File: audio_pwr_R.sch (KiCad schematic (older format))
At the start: 43 parts, among them Q201 BC546, Q202 BC546, Q203 BC546, Q204 BD140, Q205 BC546, Q206 BD139, Q207 BD140, Q208 MJL21193, Q209 MJL21194

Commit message: Lots of part changes to SMD devices. Adding MPN, MFG to all parts for BOM export.
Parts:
- removed F201, F202: 3A, Fuseholders:Fuseholder5x20_horiz_open_inline_Type-I, symbol Device:Fuse
- removed Q201, Q203: BC546, Package_TO_SOT_THT:TO-92_Inline, symbol AAMB-rescue:BC546-transistors
- added F301, F302: 0154003.DR, Fuse:0154003.DR, symbol Fuse:0154003.DR
- added U301: BC846BDW1T1G, Package_TO_SOT_SMD:SOT-363_SC-70-6, symbol OnSemi_BC846:BC846BDW1T1G
- C201: footprint Capacitor_THT:CP_Radial_D5.0mm_P2.00mm -> Capacitor_SMD:CP_Elec_4x5.4; DigiKey (none) -> https://www.we-online.de/katalog/datasheet/865080640004.pdf; MFG (none) -> Würth Elektronik; MPN (none) -> 865080640004
- C202, C204, C206: footprint Capacitor_THT:C_Disc_D5.1mm_W3.2mm_P5.00mm -> Capacitor_SMD:C_0603_1608Metric_Pad1.05x0.95mm_HandSolder; DigiKey (none) -> https://www.digikey.com/product-detail/en/w%C3%BCrth-elektr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; MFG (none) -> Würth Elektronik; MPN (none) -> 885012006057
- C203: footprint Capacitor_THT:CP_Radial_D10.0mm_P5.00mm -> Capacitor_SMD:C_Elec_5x5.4; DigiKey (none) -> https://www.digikey.com/product-detail/en/w%C3%BCrth-elektr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; MFG (none) -> Würth Elektronik; MPN (none) -> 865080142007
- C205: footprint Capacitor_THT:CP_Radial_D10.0mm_P5.00mm -> Capacitor_SMD:C_Elec_6.3x7.7; DigiKey (none) -> https://www.digikey.com/product-detail/en/w%C3%BCrth-elektr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; MFG (none) -> Würth Elektronik; MPN (none) -> 865080545012
- C207, C208, C209: DigiKey (none) -> https://www.digikey.com/product-detail/en/kemet/R82EC3100AA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; MFG (none) -> KEMET; MPN (none) -> R82EC3100AA70K
- C210, C211: footprint Capacitor_THT:CP_Radial_D10.0mm_P5.00mm -> Capacitor_SMD:CP_Elec_10x10.5; DigiKey (none) -> https://www.digikey.com/product-detail/en/nichicon/UUX1J101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; MFG (none) -> Nichicon; MPN (none) -> UUX1J101MNL1GS
- D201: footprint LED_THT:LED_D3.0mm -> LED_SMD:LED_0603_1608Metric_Pad1.05x0.95mm_HandSolder; DigiKey (none) -> https://www.digikey.com/product-detail/en/rohm-semiconducto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; MFG (none) -> Rohm Semiconductor; MPN (none) -> SML-D12U1WT86
- Q202, Q205: value BC546 -> BC846; footprint Package_TO_SOT_THT:TO-92_Inline -> Package_TO_SOT_SMD:SOT-23; DigiKey (none) -> https://www.digikey.com/product-detail/en/on-semiconductor/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; MFG (none) -> ON Semiconductor; MPN (none) -> BC846BLT1G
- Q204, Q207: value BD140 -> BCP53; footprint Package_TO_SOT_THT:TO-126-3_Vertical -> Package_TO_SOT_SMD:SOT-223; DigiKey (none) -> https://www.digikey.com/product-detail/en/on-semiconductor/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; MFG (none) -> ON Semiconductor; MPN (none) -> SBCP53-10T1G
- Q206: value BD139 -> BCP56; footprint Package_TO_SOT_THT:TO-126-3_Vertical -> Package_TO_SOT_SMD:SOT-223; DigiKey (none) -> https://www.digikey.com/product-detail/en/on-semiconductor/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; MFG (none) -> ON Semiconductor; MPN (none) -> SBCP56-16T3G
- R214, R215: value 15m -> 330m; footprint Resistor_THT:R_Axial_Power_L25.0mm_W9.0mm_P10.16mm_Vertical -> Resistor_THT:R_Radial_Power_L13.0mm_W9.0mm_P5.00mm; DigiKey (none) -> https://www.digikey.com/product-detail/en/te-connectivity-p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; MFG (none) -> TE Connectivity Passive Product; MPN (none) -> SQMW5R33J

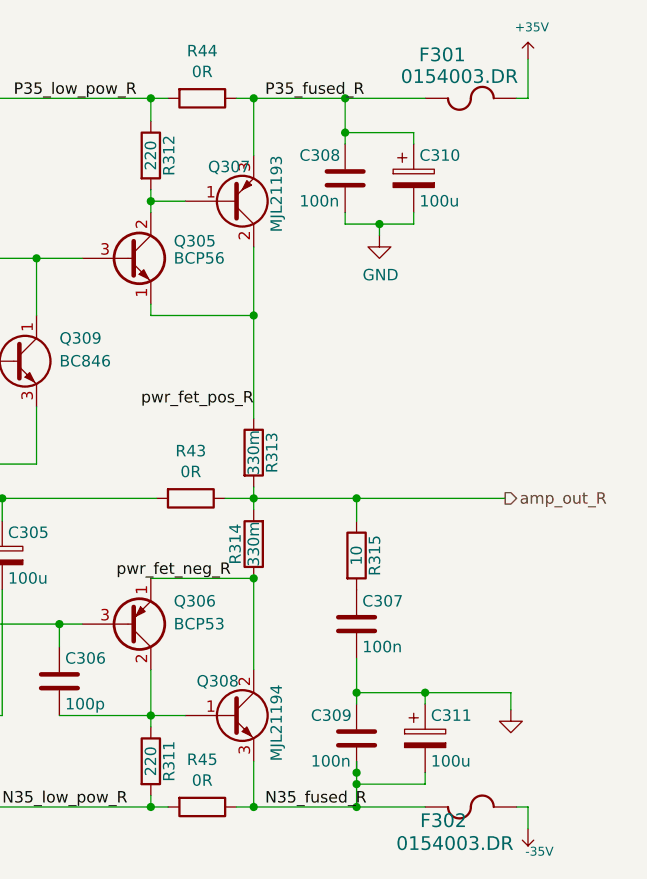
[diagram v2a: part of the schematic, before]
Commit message: Layout startover, sorting, some routing. Removed redundant fuses. BOM export.
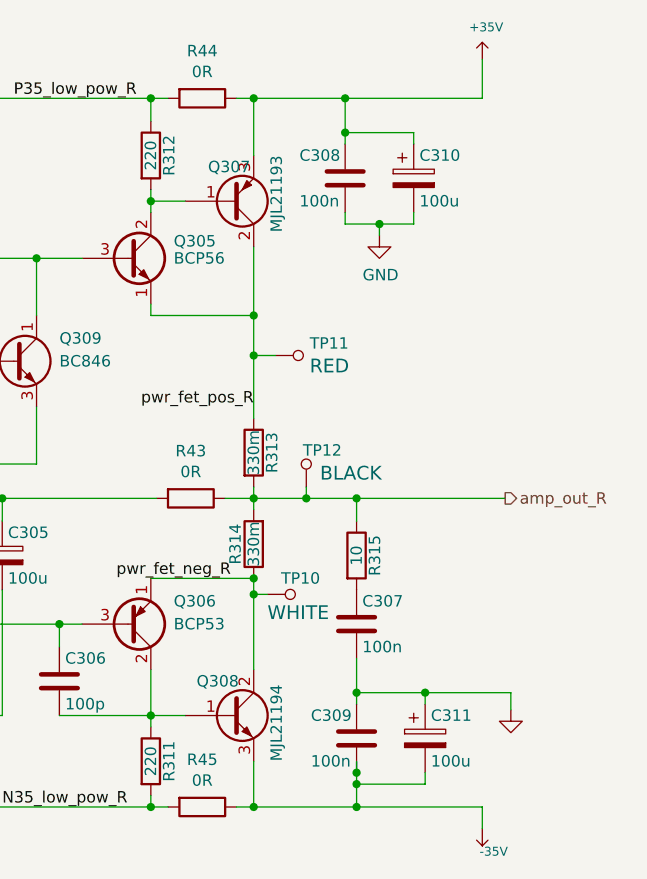
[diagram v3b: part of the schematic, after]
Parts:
- removed F301, F302: 0154003.DR, Fuse:0154003.DR, symbol Fuse:0154003.DR
- added TP10: 5002, digikey-footprints:Test_Point_D1.02mm, symbol dk_Test-Points:5002
- added TP11: 5000, digikey-footprints:Test_Point_D1.02mm, symbol dk_Test-Points:5000
- added TP12: 5001, digikey-footprints:Test_Point_D1.02mm, symbol dk_Test-Points:5001
- C201, C202, C203, C204, C205, C206: MFG Würth Elektronik -> Wurth Elektronik
- Q208: DigiKey (none) -> https://www.digikey.com/products/en/discrete-semiconductor-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; MFG (none) -> ON Semiconductor; MPN (none) -> MJL21193G
- Q209: DigiKey (none) -> https://www.digikey.com/products/en/discrete-semiconductor-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; MFG (none) -> ON Semiconductor; MPN (none) -> MJL21194G
- R201, R203, R207, R209: DigiKey (none) -> https://www.digikey.com/product-detail/en/vishay-dale/RCS06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; MFG (none) -> Vishay Dale; MPN (none) -> RCS06031K00FKEA
- R202, R204, R208: DigiKey (none) -> https://www.digikey.com/product-detail/en/te-connectivity-p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; MFG (none) -> TE Connectivity Passive Product; MPN (none) -> CRGCQ0603F22K
- R205, R206: DigiKey (none) -> https://www.digikey.com/product-detail/en/te-connectivity-p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; MFG (none) -> TE Connectivity Passive Product; MPN (none) -> CRGCQ0603F560R
- R210, R211: DigiKey (none) -> https://www.digikey.com/product-detail/en/vishay-dale/CRCW0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; MFG (none) -> Vishay Dale; MPN (none) -> CRCW06033K30FKEA
- R212, R213: DigiKey (none) -> https://www.digikey.com/product-detail/en/panasonic-electro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; MFG (none) -> Panasonic Electronic Components; MPN (none) -> ERJ-PA3F2200V
- R216: DigiKey (none) -> https://www.digikey.com/product-detail/en/panasonic-electro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; MFG (none) -> Panasonic Electronic Components; MPN (none) -> ERJ-PA3F10R0V
- R43, R44, R45: MFG (none) -> Stackpole Electronics Inc; MPN (none) -> RMCF1210ZT0R00
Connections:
- net N35_fused_R is gone; now on net -35V: C209.2, C211.2, Q209.3 (E), R45.1
- net P35_fused_R is gone; now on net +35V: C207.1, C210.1, Q208.3 (E), R44.1
- net amp_out_R: now also TP12.1
- net pwr_fet_neg_R: now also TP10.1
- net pwr_fet_pos_R: now also TP11.1

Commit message: Capturing layout progress.
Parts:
- removed C201: 4.7u, Capacitor_SMD:CP_Elec_4x5.4, symbol Device:CP
- removed TP10: 5002, digikey-footprints:Test_Point_D1.02mm, symbol dk_Test-Points:5002
- removed TP11: 5000, digikey-footprints:Test_Point_D1.02mm, symbol dk_Test-Points:5000
- removed TP12: 5001, digikey-footprints:Test_Point_D1.02mm, symbol dk_Test-Points:5001
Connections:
- net amp_in_R: now also R201.2
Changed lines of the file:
@@
-$EndComp
-$Comp
-L Device:CP C201
-U 1 1 5E1CCAE5
-P 2750 3650
-AR Path="/5C7F608F/5E1CCAE5" Ref="C201"  Part="1"
-AR Path="/5C814038/5E1CCAE5" Ref="C301"  Part="1"
-AR Path="/5E252703/5E1CCAE5" Ref="C?"  Part="1"
-F 0 "C301" H 2775 3750 50  0000 L CNN
-F 1 "4.7u" H 2775 3550 50  0000 L CNN
-F 2 "Capacitor_SMD:CP_Elec_4x5.4" H 2788 3500 50  0001 C CNN
-F 3 "https://www.digikey.com/product-detail/en/w%C3%BCrth-elektronik/865080640004/732-8449-1-ND/5728406" H 2750 3650 50  0001 C CNN
-F 4 "https://www.we-online.de/katalog/datasheet/865080640004.pdf" H 2750 3650 50  0001 C CNN "DigiKey"
-F 5 "Wurth Elektronik" H 2750 3650 50  0001 C CNN "MFG"
-F 6 "865080640004" H 2750 3650 50  0001 C CNN "MPN"
-	1    2750 3650
-	0    -1   -1   0
 $EndComp
 $Comp
@@
 Connection ~ 3000 4350
 Wire Wire Line
-	2900 3650 2950 3650
-Wire Wire Line
 	3850 4450 3850 4350
 Connection ~ 3850 4350
@@
 	6900 3600 6900 3650
 Connection ~ 6900 3650
-Wire Wire Line
-	6900 4000 6900 4070
 $Comp
 L Device:Q_PNP_BCE Q208
@@
 	6450 2350 6450 2400
 Wire Wire Line
-	6900 2850 6900 3025
-Wire Wire Line
 	7300 2050 7300 2100
 Connection ~ 3300 3800
@@
 Wire Wire Line
 	4900 4400 4900 4500
-Text HLabel 2450 3650 0    50   Input ~ 0
+Text HLabel 2750 3650 0    50   Input ~ 0
 amp_in_R
 Text HLabel 8000 3650 2    50   Output ~ 0
@@
 Wire Wire Line
 	6900 5000 7350 5000
-Wire Wire Line
-	6900 3650 7130 3650
 Connection ~ 7450 2450
 Wire Wire Line
@@
 Wire Wire Line
 	7350 4500 7350 4550
-Wire Wire Line
-	2600 3650 2450 3650
 $Comp
 L AAMB-rescue:+35V-Power-amp #PWR0110
@@
 Wire Wire Line
 	3650 3650 3800 3650
-$Comp
-L dk_Test-Points:5000 TP?
-U 1 1 5E912507
-P 7095 3025
-AR Path="/5C7F608F/5E912507" Ref="TP?"  Part="1"
-AR Path="/5C814038/5E912507" Ref="TP11"  Part="1"
-F 0 "TP11" V 7148 2975 50  0000 R CNN
-F 1 "5000" H 7095 2925 50  0001 C CNN
-F 2 "digikey-footprints:Test_Point_D1.02mm" H 7295 3225 60  0001 L CNN
-F 3 "http://www.keyelco.com/product-pdf.cfm?p=1309" H 7295 3325 60  0001 L CNN
-F 4 "36-5000-ND" H 7295 3425 60  0001 L CNN "Digi-Key_PN"
-F 5 "5000" H 7295 3525 60  0001 L CNN "MPN"
-F 6 "Test and Measurement" H 7295 3625 60  0001 L CNN "Category"
-F 7 "Test Points" H 7295 3725 60  0001 L CNN "Family"
-F 8 "http://www.keyelco.com/product-pdf.cfm?p=1309" H 7295 3825 60  0001 L CNN "DK_Datasheet_Link"
-F 9 "/product-detail/en/keystone-electronics/5000/36-5000-ND/255326" H 7295 3925 60  0001 L CNN "DK_Detail_Page"
-F 10 "RED" V 7049 2975 60  0000 R CNN "Description"
-F 11 "Keystone Electronics" H 7295 4125 60  0001 L CNN "Manufacturer"
-F 12 "Active" H 7295 4225 60  0001 L CNN "Status"
-F 13 "/product-detail/en/keystone-electronics/5000/36-5000-ND/255326" H 7095 3025 50  0001 C CNN "DigiKey"
-F 14 "Keystone Electronics" H 7095 3025 50  0001 C CNN "MFG"
-	1    7095 3025
-	0    -1   -1   0
-$EndComp
-$Comp
-L dk_Test-Points:5001 TP?
-U 1 1 5E912518
-P 7130 3500
-AR Path="/5C7F608F/5E912518" Ref="TP?"  Part="1"
-AR Path="/5C814038/5E912518" Ref="TP12"  Part="1"
-F 0 "TP12" H 7145 3440 50  0000 R CNN
-F 1 "5001" H 7130 3400 50  0001 C CNN
-F 2 "digikey-footprints:Test_Point_D1.02mm" H 7330 3700 60  0001 L CNN
-F 3 "http://www.keyelco.com/product-pdf.cfm?p=1310" H 7330 3800 60  0001 L CNN
-F 4 "36-5001-ND" H 7330 3900 60  0001 L CNN "Digi-Key_PN"
-F 5 "5001" H 7330 4000 60  0001 L CNN "MPN"
-F 6 "Test and Measurement" H 7330 4100 60  0001 L CNN "Category"
-F 7 "Test Points" H 7330 4200 60  0001 L CNN "Family"
-F 8 "http://www.keyelco.com/product-pdf.cfm?p=1310" H 7330 4300 60  0001 L CNN "DK_Datasheet_Link"
-F 9 "/product-detail/en/keystone-electronics/5001/36-5001-ND/255327" H 7330 4400 60  0001 L CNN "DK_Detail_Page"
-F 10 "BLACK" H 7070 3540 60  0000 R CNN "Description"
-F 11 "Keystone Electronics" H 7330 4600 60  0001 L CNN "Manufacturer"
-F 12 "Active" H 7330 4700 60  0001 L CNN "Status"
-F 13 "/product-detail/en/keystone-electronics/5001/36-5001-ND/255327" H 7130 3500 50  0001 C CNN "DigiKey"
-F 14 "Keystone Electronics" H 7130 3500 50  0001 C CNN "MFG"
-	1    7130 3500
-	-1   0    0    1
-$EndComp
-$Comp
-L dk_Test-Points:5002 TP?
-U 1 1 5E912529
-P 7060 4070
-AR Path="/5C7F608F/5E912529" Ref="TP?"  Part="1"
-AR Path="/5C814038/5E912529" Ref="TP10"  Part="1"
-F 0 "TP10" V 7130 4110 50  0000 R CNN
-F 1 "5002" H 7060 3970 50  0001 C CNN
-F 2 "digikey-footprints:Test_Point_D1.02mm" H 7260 4270 60  0001 L CNN
-F 3 "http://www.keyelco.com/product-pdf.cfm?p=1311" H 7260 4370 60  0001 L CNN
-F 4 "36-5002-ND" H 7260 4470 60  0001 L CNN "Digi-Key_PN"
-F 5 "5002" H 7260 4570 60  0001 L CNN "MPN"
-F 6 "Test and Measurement" H 7260 4670 60  0001 L CNN "Category"
-F 7 "Test Points" H 7260 4770 60  0001 L CNN "Family"
-F 8 "http://www.keyelco.com/product-pdf.cfm?p=1311" H 7260 4870 60  0001 L CNN "DK_Datasheet_Link"
-F 9 "/product-detail/en/keystone-electronics/5002/36-5002-ND/255328" H 7260 4970 60  0001 L CNN "DK_Detail_Page"
-F 10 "WHITE" V 6980 4170 60  0000 R CNN "Description"
-F 11 "Keystone Electronics" H 7260 5170 60  0001 L CNN "Manufacturer"
-F 12 "Active" H 7260 5270 60  0001 L CNN "Status"
-F 13 "/product-detail/en/keystone-electronics/5002/36-5002-ND/255328" H 7060 4070 50  0001 C CNN "DigiKey"
-F 14 "Keystone Electronics" H 7060 4070 50  0001 C CNN "MFG"
-	1    7060 4070
-	0    -1   -1   0
-$EndComp
-Connection ~ 6900 3025
-Wire Wire Line
-	6900 3025 6900 3300
-Wire Wire Line
-	6995 3025 6900 3025
-Wire Wire Line
-	7130 3600 7130 3650
-Connection ~ 7130 3650
-Wire Wire Line
-	7130 3650 7350 3650
-Wire Wire Line
-	6960 4070 6900 4070
-Connection ~ 6900 4070
-Wire Wire Line
-	6900 4070 6900 4400
 Wire Wire Line
 	7300 1900 7900 1900
 Wire Wire Line
 	7350 5000 7900 5000
+Wire Wire Line
+	6900 3650 7350 3650
+Wire Wire Line
+	6900 2850 6900 3300
+Wire Wire Line
+	6900 4000 6900 4400
+Wire Wire Line
+	2750 3650 2950 3650
 $EndSCHEMATC

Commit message: Place and route complete. Silkscreen cleanup needed.
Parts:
- VR201: footprint Murata-POT:PV36W202C01B00 -> Potentiometer_THT:Potentiometer_Bourns_3296W_Vertical; DigiKey (none) -> https://www.digikey.com/product-detail/en/bourns-inc/3296W-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; MFG (none) -> Bourns Inc.; MPN (none) -> 3296W-1-202LF
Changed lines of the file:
@@
 F 0 "VR301" V 5350 3250 50  0000 C CNN
 F 1 "2k" V 5450 3250 50  0000 C CNN
-F 2 "Murata-POT:PV36W202C01B00" H 5450 3250 50  0001 C CNN
-F 3 "" H 5450 3250 50  0001 C CNN
+F 2 "Potentiometer_THT:Potentiometer_Bourns_3296W_Vertical" H 5450 3250 50  0001 C CNN
+F 3 "https://www.bourns.com/docs/Product-Datasheets/3296.pdf" H 5450 3250 50  0001 C CNN
+F 4 "https://www.digikey.com/product-detail/en/bourns-inc/3296W-1-202LF/3296W-202LF-ND/1088050" V 5450 3250 50  0001 C CNN "DigiKey"
+F 5 "Bourns Inc." V 5450 3250 50  0001 C CNN "MFG"
+F 6 "3296W-1-202LF" V 5450 3250 50  0001 C CNN "MPN"
 	1    5450 3250
 	1    0    0    -1

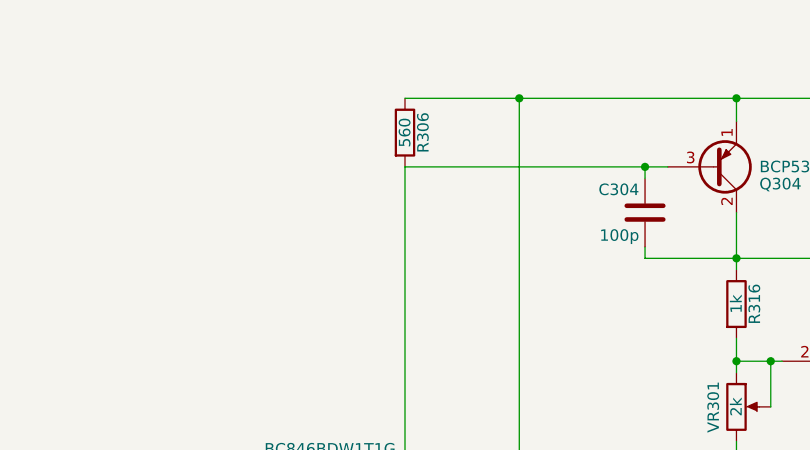
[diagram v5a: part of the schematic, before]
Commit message: Layout complete. Screw holes added and connected to GND.
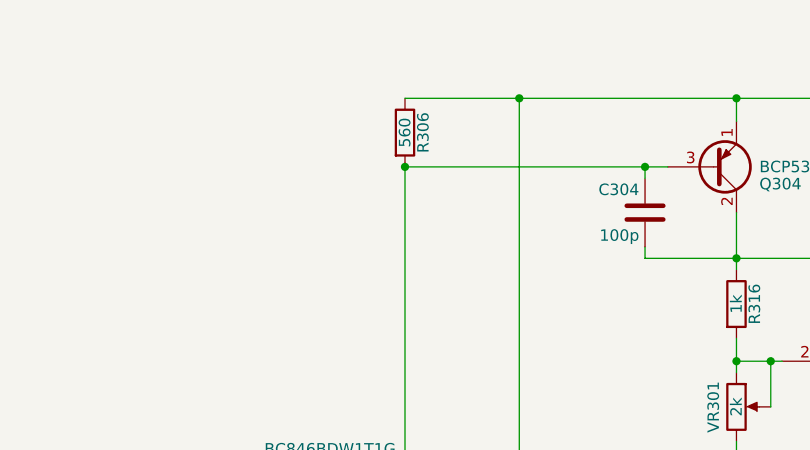
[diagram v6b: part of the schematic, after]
